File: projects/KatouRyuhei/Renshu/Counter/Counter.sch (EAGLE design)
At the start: 63 parts

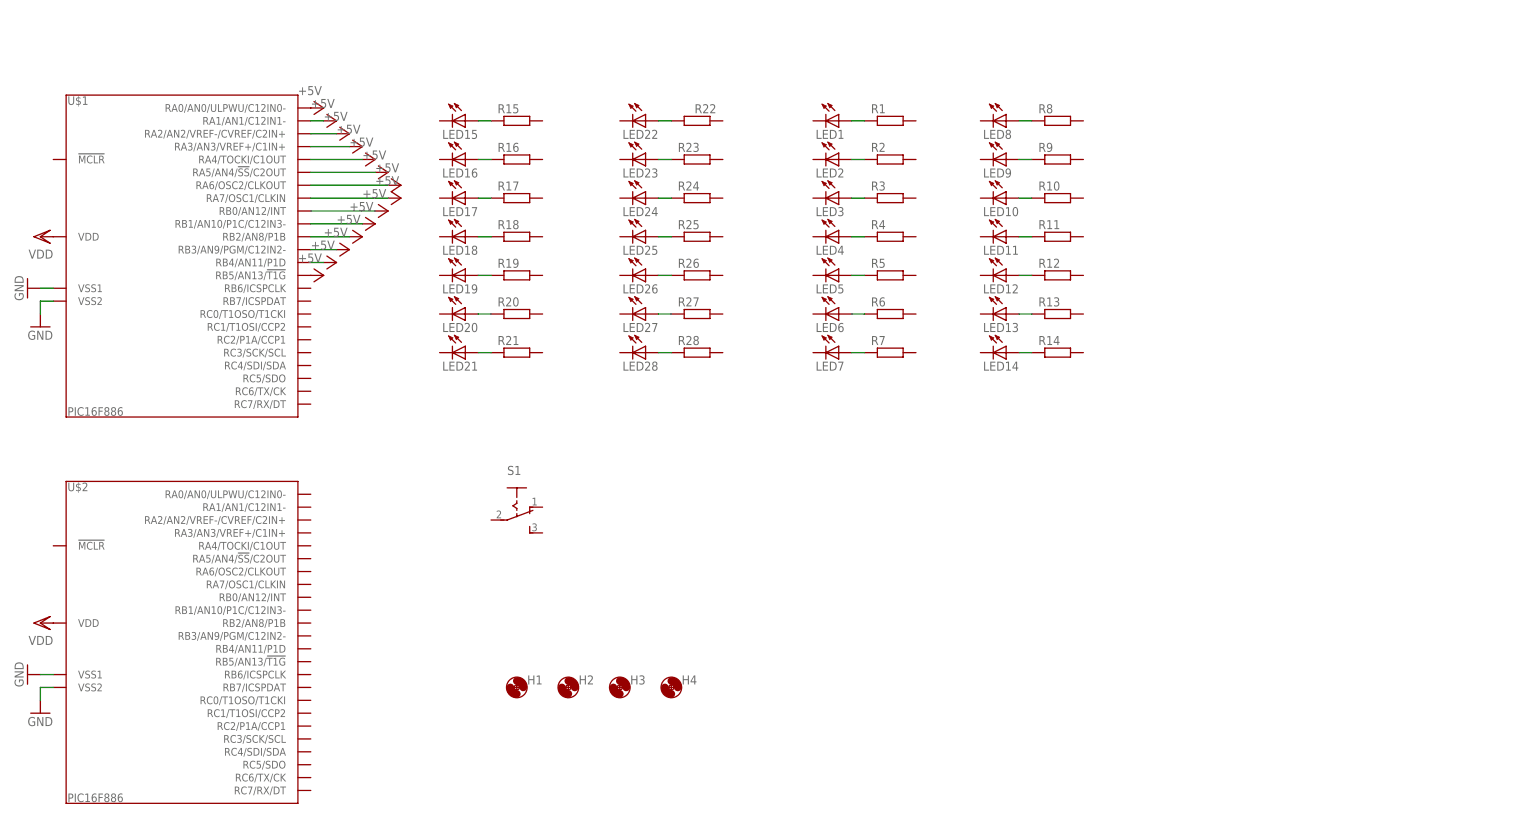
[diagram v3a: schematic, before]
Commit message: 10進数2桁カウンタ製作途中
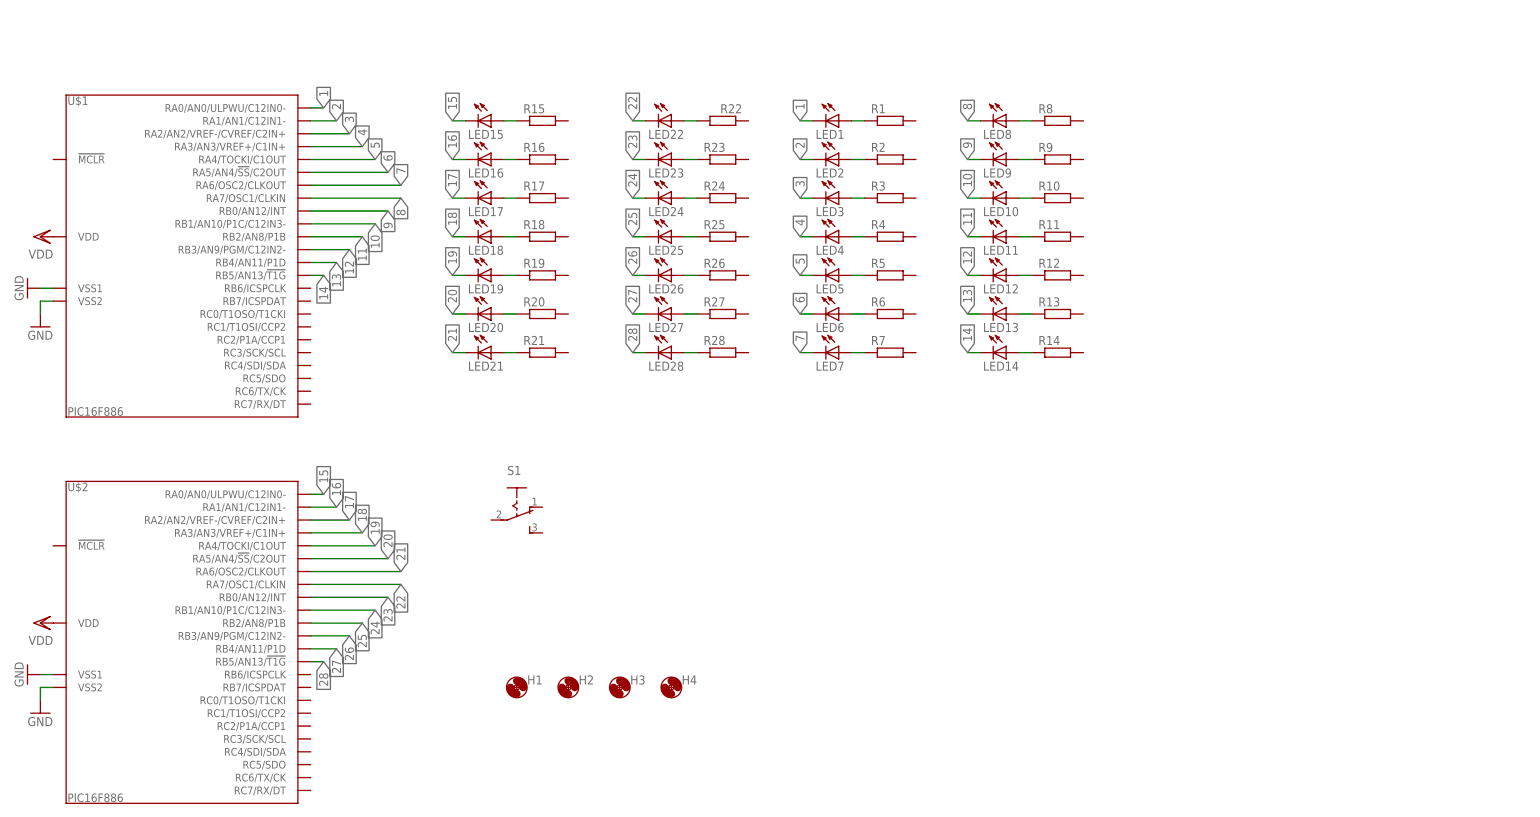
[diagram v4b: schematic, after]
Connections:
- removed net +5V: U$1.RA0/AN0/ULPWU/C12IN0-, U$1.RA1/AN1/C12IN1-, U$1.RA2/AN2/VREF-/CVREF/C2IN+, U$1.RA3/AN3/VREF+/C1IN+, U$1.RA4/TOCKI/C1OUT, U$1.RA5/AN4/!SS!/C2OUT, U$1.RA6/OSC2/CLKOUT, U$1.RA7/OSC1/CLKIN, U$1.RB0/AN12/INT, U$1.RB1/AN10/P1C/C12IN3-, U$1.RB2/AN8/P1B, U$1.RB3/AN9/PGM/C12IN2-, U$1.RB4/AN11/P1D, U$1.RB5/AN13/!T1G
- new net 1: LED1.C, U$1.RA0/AN0/ULPWU/C12IN0-
- new net 10: LED10.C, U$1.RB1/AN10/P1C/C12IN3-
- new net 11: LED11.C, U$1.RB2/AN8/P1B
- new net 12: LED12.C, U$1.RB3/AN9/PGM/C12IN2-
- new net 13: LED13.C, U$1.RB4/AN11/P1D
- new net 14: LED14.C, U$1.RB5/AN13/!T1G
- new net 15: LED15.C
- new net 16: LED16.C
- new net 17: LED17.C
- new net 18: LED18.C
- new net 19: LED19.C
- new net 2: LED2.C, U$1.RA1/AN1/C12IN1-
- new net 20: LED20.C
- new net 21: LED21.C
- new net 22: LED22.C
- new net 23: LED23.C
- new net 24: LED24.C
- new net 25: LED25.C
- new net 26: LED26.C
- new net 27: LED27.C
- new net 28: LED28.C
- new net 3: LED3.C, U$1.RA2/AN2/VREF-/CVREF/C2IN+
- new net 4: LED4.C, U$1.RA3/AN3/VREF+/C1IN+
- new net 5: LED5.C, U$1.RA4/TOCKI/C1OUT
- new net 6: LED6.C, U$1.RA5/AN4/!SS!/C2OUT
- new net 7: LED7.C, U$1.RA6/OSC2/CLKOUT
- new net 8: LED8.C, U$1.RA7/OSC1/CLKIN
- new net 9: LED9.C, U$1.RB0/AN12/INT
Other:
- moved on the sheet: LED15, LED16, LED17, LED18, LED19, LED20, LED21, LED22, LED23, LED24, LED25, LED26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

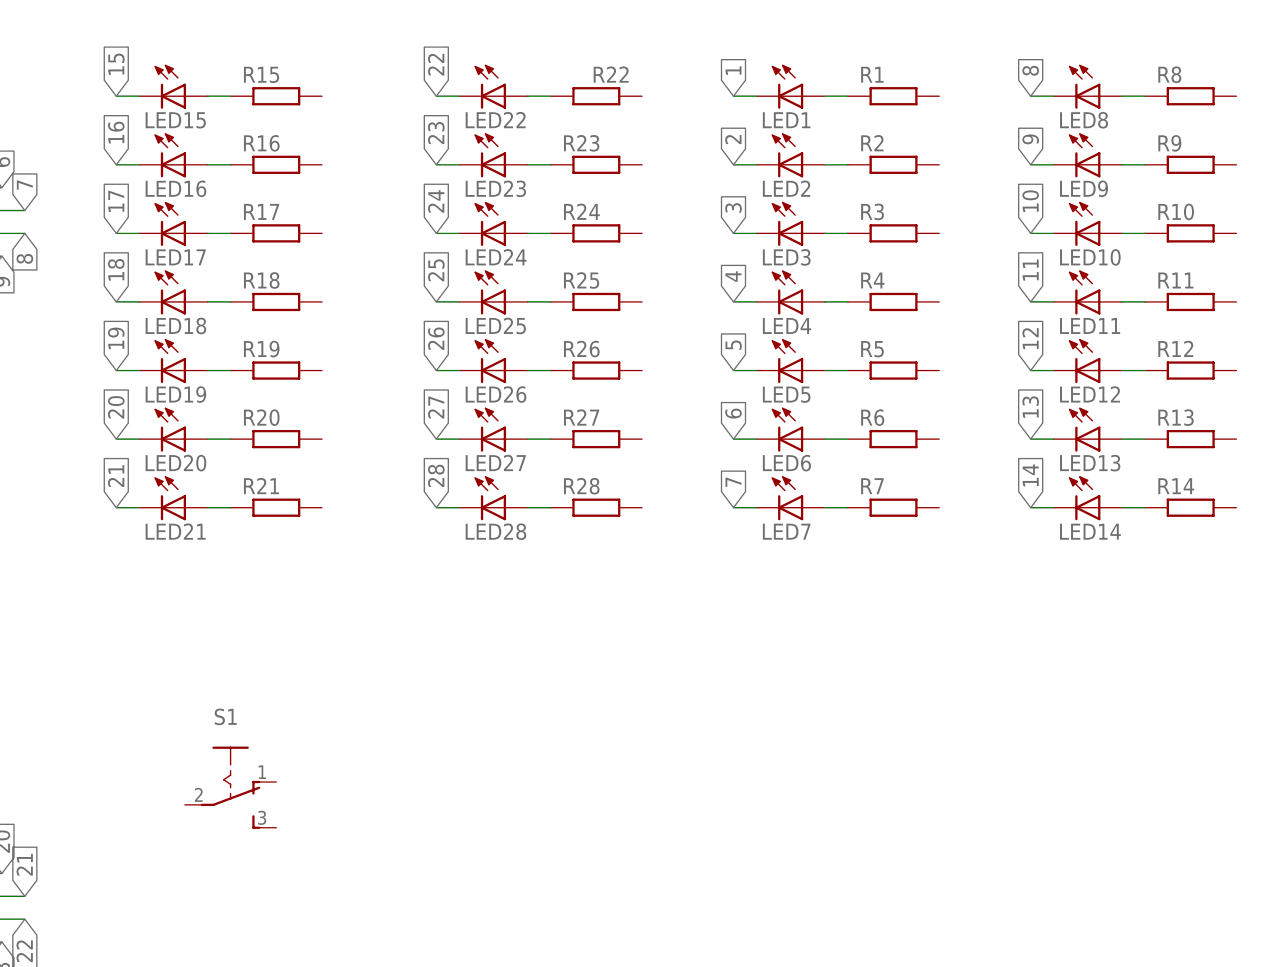
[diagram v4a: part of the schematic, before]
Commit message: 10進数2桁カウンタ製作途中
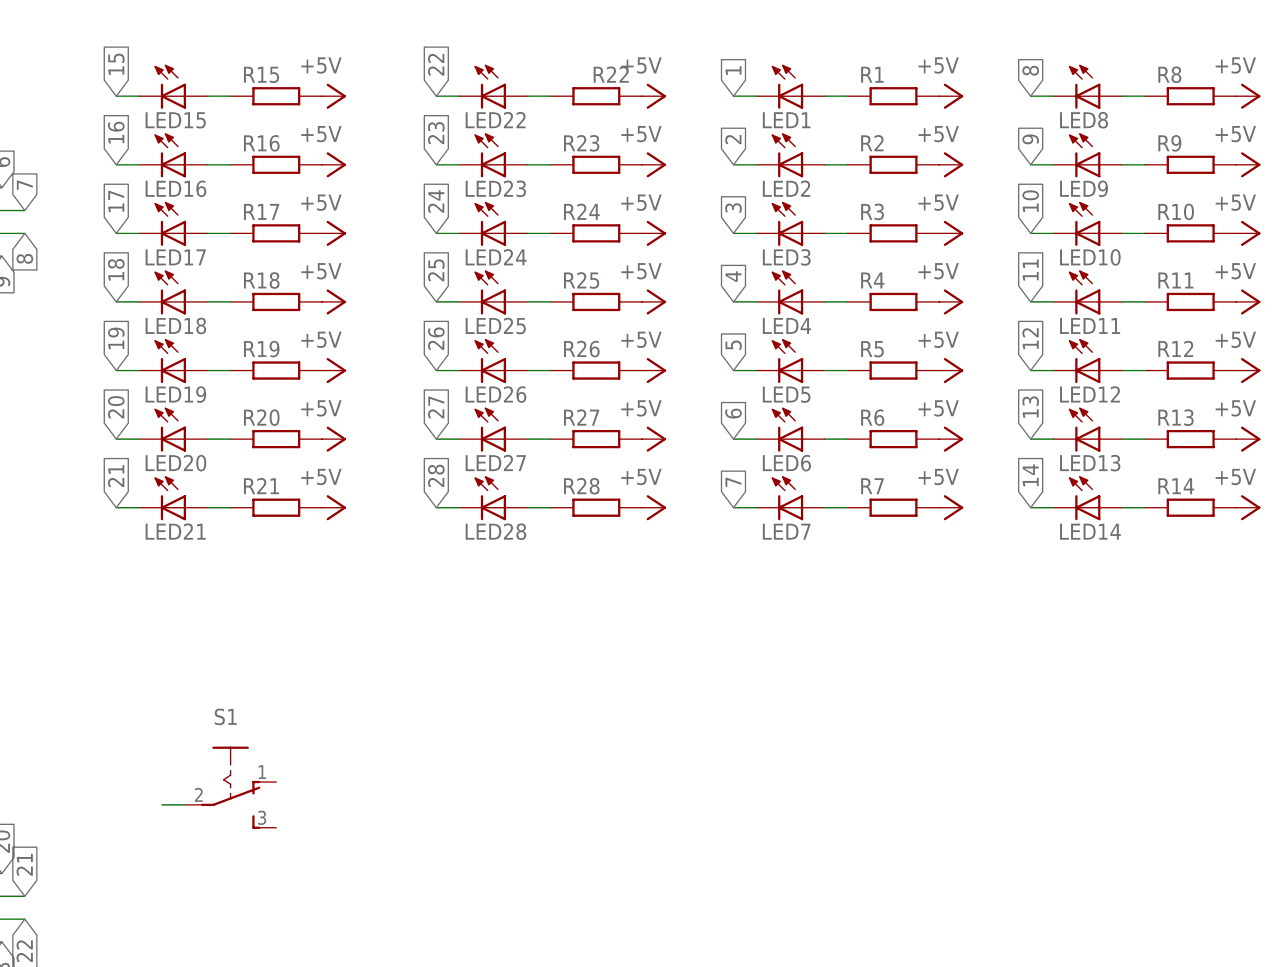
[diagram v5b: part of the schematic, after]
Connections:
- new net +5V: R1.2, R10.2, R11.2, R12.2, R13.2, R14.2, R15.2, R16.2, R17.2, R18.2, R19.2, R2.2, R20.2, R21.2, R22.1, R23.2, R24.2, R25.2, R26.2, R27.2, R28.2, R3.2, R4.2, R5.2, R6.2, R7.2, R8.2, R9.2
- new net N$29: S1.2
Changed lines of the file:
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@@
 <part name="GND3" library="supply1" deviceset="GND" device=""/>
 <part name="GND4" library="supply1" deviceset="GND" device=""/>
+<part name="P+1" library="supply1" deviceset="+5V" device=""/>
+<part name="P+2" library="supply1" deviceset="+5V" device=""/>
+<part name="P+3" library="supply1" deviceset="+5V" device=""/>
+<part name="P+4" library="supply1" deviceset="+5V" device=""/>
+<part name="P+5" library="supply1" deviceset="+5V" device=""/>
+<part name="P+6" library="supply1" deviceset="+5V" device=""/>
+<part name="P+7" library="supply1" deviceset="+5V" device=""/>
+<part name="P+8" library="supply1" deviceset="+5V" device=""/>
+<part name="P+9" library="supply1" deviceset="+5V" device=""/>
+<part name="P+10" library="supply1" deviceset="+5V" device=""/>
+<part name="P+11" library="supply1" deviceset="+5V" device=""/>
+<part name="P+12" library="supply1" deviceset="+5V" device=""/>
+<part name="P+13" library="supply1" deviceset="+5V" device=""/>
+<part name="P+14" library="supply1" deviceset="+5V" device=""/>
+<part name="P+15" library="supply1" deviceset="+5V" device=""/>
+<part name="P+16" library="supply1" deviceset="+5V" device=""/>
+<part name="P+17" library="supply1" deviceset="+5V" device=""/>
+<part name="P+18" library="supply1" deviceset="+5V" device=""/>
+<part name="P+19" library="supply1" deviceset="+5V" device=""/>
+<part name="P+20" library="supply1" deviceset="+5V" device=""/>
+<part name="P+21" library="supply1" deviceset="+5V" device=""/>
+<part name="P+22" library="supply1" deviceset="+5V" device=""/>
+<part name="P+23" library="supply1" deviceset="+5V" device=""/>
+<part name="P+24" library="supply1" deviceset="+5V" device=""/>
+<part name="P+25" library="supply1" deviceset="+5V" device=""/>
+<part name="P+26" library="supply1" deviceset="+5V" device=""/>
+<part name="P+27" library="supply1" deviceset="+5V" device=""/>
+<part name="P+28" library="supply1" deviceset="+5V" device=""/>
 </parts>
 <sheets>
@@
 <instance part="GND3" gate="1" x="-218.44" y="17.78" rot="R270"/>
 <instance part="GND4" gate="1" x="-215.9" y="10.16"/>
+<instance part="P+1" gate="1" x="-109.22" y="81.28" rot="R270"/>
+<instance part="P+2" gate="1" x="-109.22" y="88.9" rot="R270"/>
+<instance part="P+3" gate="1" x="-109.22" y="96.52" rot="R270"/>
+<instance part="P+4" gate="1" x="-109.22" y="104.14" rot="R270"/>
+<instance part="P+5" gate="1" x="-109.22" y="111.76" rot="R270"/>
+<instance part="P+6" gate="1" x="-109.22" y="119.38" rot="R270"/>
+<instance part="P+7" gate="1" x="-109.22" y="127" rot="R270"/>
+<instance part="P+8" gate="1" x="-73.66" y="127" rot="R270"/>
+<instance part="P+9" gate="1" x="-73.66" y="119.38" rot="R270"/>
+<instance part="P+10" gate="1" x="-73.66" y="111.76" rot="R270"/>
+<instance part="P+11" gate="1" x="-73.66" y="104.14" rot="R270"/>
+<instance part="P+12" gate="1" x="-73.66" y="96.52" rot="R270"/>
+<instance part="P+13" gate="1" x="-73.66" y="88.9" rot="R270"/>
+<instance part="P+14" gate="1" x="-73.66" y="81.28" rot="R270"/>
+<instance part="P+15" gate="1" x="-40.64" y="81.28" rot="R270"/>
+<instance part="P+16" gate="1" x="-40.64" y="88.9" rot="R270"/>
+<instance part="P+17" gate="1" x="-40.64" y="96.52" rot="R270"/>
+<instance part="P+18" gate="1" x="-40.64" y="104.14" rot="R270"/>
+<instance part="P+19" gate="1" x="-40.64" y="111.76" rot="R270"/>
+<instance part="P+20" gate="1" x="-40.64" y="119.38" rot="R270"/>
+<instance part="P+21" gate="1" x="-40.64" y="127" rot="R270"/>
+<instance part="P+22" gate="1" x="-7.62" y="127" rot="R270"/>
+<instance part="P+23" gate="1" x="-7.62" y="119.38" rot="R270"/>
+<instance part="P+24" gate="1" x="-7.62" y="111.76" rot="R270"/>
+<instance part="P+25" gate="1" x="-7.62" y="104.14" rot="R270"/>
+<instance part="P+26" gate="1" x="-7.62" y="96.52" rot="R270"/>
+<instance part="P+27" gate="1" x="-7.62" y="88.9" rot="R270"/>
+<instance part="P+28" gate="1" x="-7.62" y="81.28" rot="R270"/>
 </instances>
 <busses>
@@
 </segment>
 </net>
+<net name="N$29" class="0">
+<segment>
+<pinref part="S1" gate="1" pin="2"/>
+<wire x1="-127" y1="48.26" x2="-129.54" y2="48.26" width="0.1524" layer="91"/>
+</segment>
+</net>
+<net name="+5V" class="0">
+<segment>
+<pinref part="R21" gate="G$1" pin="2"/>
+<pinref part="P+1" gate="1" pin="+5V"/>
+</segment>
+<segment>
+<pinref part="R20" gate="G$1" pin="2"/>
+<pinref part="P+2" gate="1" pin="+5V"/>
+</segment>
+<segment>
+<pinref part="R19" gate="G$1" pin="2"/>
+<pinref part="P+3" gate="1" pin="+5V"/>
+</segment>
+<segment>
+<pinref part="R18" gate="G$1" pin="2"/>
+<pinref part="P+4" gate="1" pin="+5V"/>
+</segment>
+<segment>
+<pinref part="R17" gate="G$1" pin="2"/>
+<pinref part="P+5" gate="1" pin="+5V"/>
+</segment>
+<segment>
+<pinref part="R16" gate="G$1" pin="2"/>
+<pinref part="P+6" gate="1" pin="+5V"/>
+</segment>
+<segment>
+<pinref part="R15" gate="G$1" pin="2"/>
+<pinref part="P+7" gate="1" pin="+5V"/>
+</segment>
+<segment>
+<pinref part="R22" gate="G$1" pin="1"/>
+<pinref part="P+8" gate="1" pin="+5V"/>
+</segment>
+<segment>
+<pinref part="R23" gate="G$1" pin="2"/>
+<pinref part="P+9" gate="1" pin="+5V"/>
+</segment>
+<segment>
+<pinref part="R24" gate="G$1" pin="2"/>
+<pinref part="P+10" gate="1" pin="+5V"/>
+</segment>
+<segment>
+<pinref part="R25" gate="G$1" pin="2"/>
+<pinref part="P+11" gate="1" pin="+5V"/>
+</segment>
+<segment>
+<pinref part="R26" gate="G$1" pin="2"/>
+<pinref part="P+12" gate="1" pin="+5V"/>
+</segment>
+<segment>
+<pinref part="R27" gate="G$1" pin="2"/>
+<pinref part="P+13" gate="1" pin="+5V"/>
+</segment>
+<segment>
+<pinref part="R28" gate="G$1" pin="2"/>
+<pinref part="P+14" gate="1" pin="+5V"/>
+</segment>
+<segment>
+<pinref part="R7" gate="G$1" pin="2"/>
+<pinref part="P+15" gate="1" pin="+5V"/>
+</segment>
+<segment>
+<pinref part="R6" gate="G$1" pin="2"/>
+<pinref part="P+16" gate="1" pin="+5V"/>
+</segment>
+<segment>
+<pinref part="R5" gate="G$1" pin="2"/>
+<pinref part="P+17" gate="1" pin="+5V"/>
+</segment>
+<segment>
+<pinref part="R4" gate="G$1" pin="2"/>
+<pinref part="P+18" gate="1" pin="+5V"/>
+</segment>
+<segment>
+<pinref part="R3" gate="G$1" pin="2"/>
+<pinref part="P+19" gate="1" pin="+5V"/>
+</segment>
+<segment>
+<pinref part="R2" gate="G$1" pin="2"/>
+<pinref part="P+20" gate="1" pin="+5V"/>
+</segment>
+<segment>
+<pinref part="R1" gate="G$1" pin="2"/>
+<pinref part="P+21" gate="1" pin="+5V"/>
+</segment>
+<segment>
+<pinref part="R8" gate="G$1" pin="2"/>
+<pinref part="P+22" gate="1" pin="+5V"/>
+</segment>
+<segment>
+<pinref part="R9" gate="G$1" pin="2"/>
+<pinref part="P+23" gate="1" pin="+5V"/>
+</segment>
+<segment>
+<pinref part="R10" gate="G$1" pin="2"/>
+<pinref part="P+24" gate="1" pin="+5V"/>
+</segment>
+<segment>
+<pinref part="R11" gate="G$1" pin="2"/>
+<pinref part="P+25" gate="1" pin="+5V"/>
+</segment>
+<segment>
+<pinref part="R12" gate="G$1" pin="2"/>
+<pinref part="P+26" gate="1" pin="+5V"/>
+</segment>
+<segment>
+<pinref part="R13" gate="G$1" pin="2"/>
+<pinref part="P+27" gate="1" pin="+5V"/>
+</segment>
+<segment>
+<pinref part="R14" gate="G$1" pin="2"/>
+<pinref part="P+28" gate="1" pin="+5V"/>
+</segment>
+</net>
